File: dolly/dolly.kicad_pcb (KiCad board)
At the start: 2 copper layers, 71.1 x 62.2 mm, 67 parts, among them J1 USB_OTG, J10 X_End, J11 Y_End, J12 Z_End, J13 GS2, J14 GS2, J15 GS2, J16 GS2, J17 GS2, J18 GS2, J19 GS2, J2 Barrel_Jack, J20 GS2, J21 GS2, J22 X_Stepper, J23 Y_Stepper, J24 Z_Stepper, J3 UART, J4 RX, J5 TX, J6 24V_Out, J7 Probe, J8 Spindle, J9 ICSP, SW1 SW_SPST, U1 ATMEGA328PB-AU, U2 CH340G, U3 L7805, U4 AP1117-15, U5 ITEAD_HC-05, Y1 12M, Y2 16M

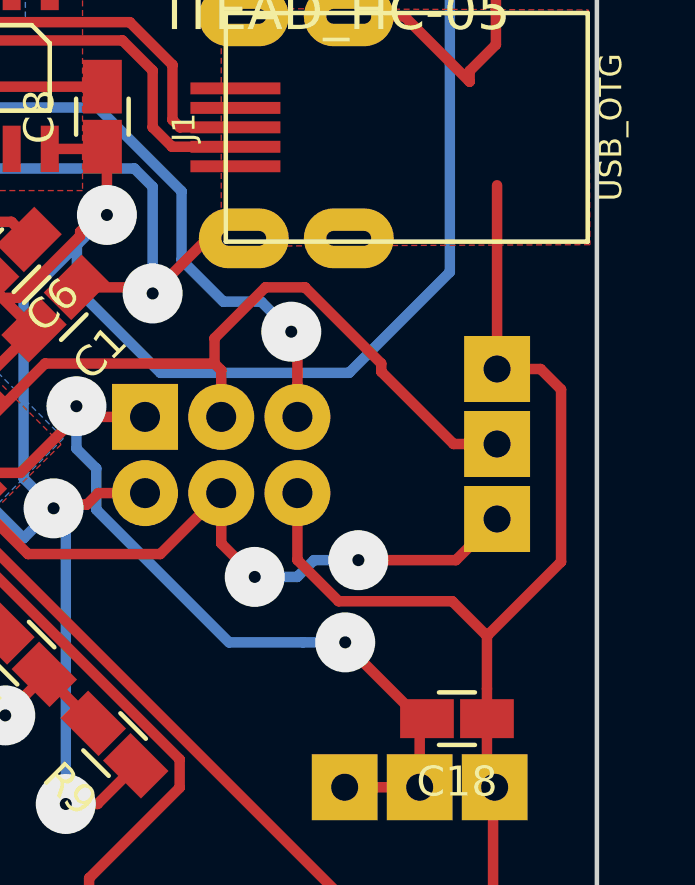
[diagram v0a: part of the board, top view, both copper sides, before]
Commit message: Adding optional 0.1uF capacitors between spindle direction/pwm pins and gnd.
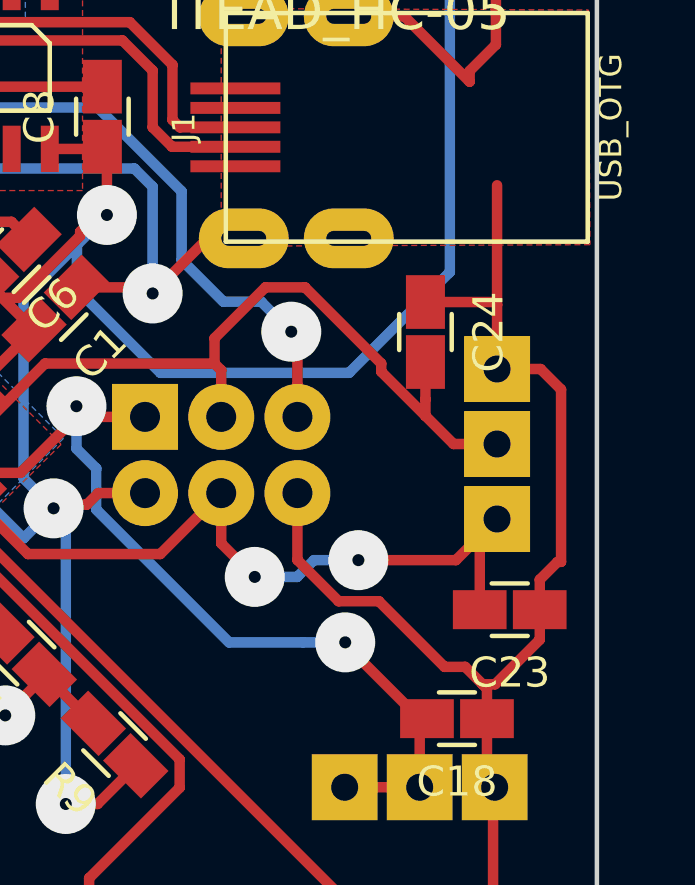
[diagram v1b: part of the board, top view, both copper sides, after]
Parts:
- added C23: 0.1u, coddingtonbear:0805_Milling, F.Cu at (202.2, 117.5)
- added C24: 0.1u, coddingtonbear:0805_Milling, F.Cu at (199.4, 108.2)
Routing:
- net GND: track 453.2 -> 456.6 mm
- net MOSI: track 22.4 -> 25.7 mm
- net SCK: track 23.7 -> 25.4 mm
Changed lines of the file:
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@@
     (thickness 1.6)
     (drawings 6)
-    (tracks 793)
+    (tracks 808)
     (zones 0)
-    (modules 67)
+    (modules 69)
     (nets 108)
   )
@@
     (add_net ~ENABLE_STEPPER)
   )
+  (module coddingtonbear:0805_Milling (layer F.Cu)
+    (at 199.39 108.22 270)
+    (descr "Resistor SMD 0805, reflow soldering, Vishay (see dcrcw.pdf)")
+    (tags "resistor 0805")
+    (attr smd)
+    (fp_text reference C24 (at 0 -2.1 270) (layer F.SilkS)
+      (effects (font (size 1 1) (thickness 0.15)))
+    )
+    (fp_text value 0.1u (at 0 2.1 270) (layer F.Fab)
+      (effects (font (size 1 1) (thickness 0.15)))
+    )
+    (fp_line (start 0.6 0.875) (end -0.6 0.875) (layer F.SilkS) (width 0.15))
+    (fp_line (start -0.6 -0.875) (end 0.6 -0.875) (layer F.SilkS) (width 0.15))
+    (pad 1 smd rect (at -1 0 270) (size 1.79 1.3) (layers F.Cu F.Paste F.Mask)
+      (net 5 GND))
+    (pad 2 smd rect (at 1 0 270) (size 1.79 1.3) (layers F.Cu F.Paste F.Mask)
+      (net 17 SCK))
+    (model Resistors_SMD.3dshapes/R_0805.wrl
+      (at (xyz 0 0 0))
+      (scale (xyz 1 1 1))
+      (rotate (xyz 0 0 0))
+    )
+  )
+  (module coddingtonbear:0805_Milling (layer F.Cu)
+    (at 202.2 117.475 180)
+    (descr "Resistor SMD 0805, reflow soldering, Vishay (see dcrcw.pdf)")
+    (tags "resistor 0805")
+    (attr smd)
+    (fp_text reference C23 (at 0 -2.1 180) (layer F.SilkS)
+      (effects (font (size 1 1) (thickness 0.15)))
+    )
+    (fp_text value 0.1u (at 0 2.1 180) (layer F.Fab)
+      (effects (font (size 1 1) (thickness 0.15)))
+    )
+    (fp_line (start -0.6 -0.875) (end 0.6 -0.875) (layer F.SilkS) (width 0.15))
+    (fp_line (start 0.6 0.875) (end -0.6 0.875) (layer F.SilkS) (width 0.15))
+    (pad 2 smd rect (at 1 0 180) (size 1.79 1.3) (layers F.Cu F.Paste F.Mask)
+      (net 15 MOSI))
+    (pad 1 smd rect (at -1 0 180) (size 1.79 1.3) (layers F.Cu F.Paste F.Mask)
+      (net 5 GND))
+    (model Resistors_SMD.3dshapes/R_0805.wrl
+      (at (xyz 0 0 0))
+      (scale (xyz 1 1 1))
+      (rotate (xyz 0 0 0))
+    )
+  )
   (module celeritous/KiCad.pretty:CAPACITOR_TANTALUM_C (layer F.Cu)
     (at 164.465 76.835 180)
@@
   (segment (start 190.0428 113.5888) (end 188.487166 113.5888) (width 0.35) (layer F.Cu) (net 4))
   (segment (start 188.487166 113.5888) (end 188.106166 113.9698) (width 0.35) (layer F.Cu) (net 4))
+  (segment (start 203.2 117.475) (end 203.2 116.475) (width 0.35) (layer F.Cu) (net 5))
+  (segment (start 203.2 116.475) (end 203.794234 115.880766) (width 0.35) (layer F.Cu) (net 5))
+  (segment (start 203.794234 115.880766) (end 203.9112 115.880766) (width 0.35) (layer F.Cu) (net 5))
+  (segment (start 200.7136 119.38) (end 201.295 119.9614) (width 0.35) (layer F.Cu) (net 5))
+  (segment (start 201.295 119.9614) (end 201.4408 120.1072) (width 0.35) (layer F.Cu) (net 5))
+  (segment (start 203.2 117.475) (end 203.2 118.475) (width 0.35) (layer F.Cu) (net 5))
+  (segment (start 201.7136 119.9614) (end 201.295 119.9614) (width 0.35) (layer F.Cu) (net 5))
+  (segment (start 203.2 118.475) (end 201.7136 119.9614) (width 0.35) (layer F.Cu) (net 5))
+  (segment (start 200.025 119.38) (end 200.7136 119.38) (width 0.35) (layer F.Cu) (net 5))
+  (segment (start 197.839001 117.194001) (end 200.025 119.38) (width 0.35) (layer F.Cu) (net 5))
+  (segment (start 196.497199 117.194001) (end 197.839001 117.194001) (width 0.35) (layer F.Cu) (net 5))
+  (segment (start 201.7776 109.4524) (end 201.7776 107.315) (width 0.35) (layer F.Cu) (net 5))
+  (segment (start 201.7776 107.315) (end 201.7776 103.3272) (width 0.35) (layer F.Cu) (net 5))
+  (segment (start 199.39 107.22) (end 201.6826 107.22) (width 0.35) (layer F.Cu) (net 5))
+  (segment (start 201.6826 107.22) (end 201.7776 107.315) (width 0.35) (layer F.Cu) (net 5))
   (segment (start 179.500731 106.517587) (end 180.858013 106.517587) (width 0.35) (layer B.Cu) (net 5))
   (segment (start 180.858013 106.517587) (end 182.9816 104.394) (width 0.35) (layer B.Cu) (net 5))
@@
   (segment (start 190.2968 106.934) (end 190.2968 103.378) (width 0.35) (layer B.Cu) (net 5))
   (segment (start 183.981599 103.394001) (end 182.9816 104.394) (width 0.35) (layer B.Cu) (net 5))
-  (segment (start 201.7776 109.4524) (end 201.7776 103.3272) (width 0.35) (layer F.Cu) (net 5))
-  (segment (start 196.497199 117.194001) (end 200.283635 117.194001) (width 0.35) (layer F.Cu) (net 5))
-  (segment (start 200.283635 117.194001) (end 201.4408 118.351166) (width 0.35) (layer F.Cu) (net 5))
   (segment (start 195.1228 113.5888) (end 195.1228 115.819602) (width 0.35) (layer F.Cu) (net 5))
   (segment (start 195.1228 115.819602) (end 196.497199 117.194001) (width 0.35) (layer F.Cu) (net 5))
   (segment (start 203.9112 110.136) (end 203.9112 115.880766) (width 0.35) (layer F.Cu) (net 5))
-  (segment (start 203.9112 115.880766) (end 201.4408 118.351166) (width 0.35) (layer F.Cu) (net 5))
   (segment (start 201.7776 109.4524) (end 203.2276 109.4524) (width 0.35) (layer F.Cu) (net 5))
   (segment (start 203.2276 109.4524) (end 203.9112 110.136) (width 0.35) (layer F.Cu) (net 5))
-  (segment (start 201.4408 118.351166) (end 201.4408 120.1072) (width 0.35) (layer F.Cu) (net 5))
   (segment (start 201.4408 120.1072) (end 201.4408 121.1072) (width 0.35) (layer F.Cu) (net 5))
   (segment (start 201.644 129.1844) (end 201.644 123.4468) (width 0.35) (layer F.Cu) (net 5))
@@
   (segment (start 199.2484 129.58) (end 199.644 129.1844) (width 0.35) (layer F.Cu) (net 14))
   (segment (start 196.7484 131.572) (end 199.2484 131.572) (width 0.35) (layer F.Cu) (net 14))
+  (segment (start 201.2 117.475) (end 201.2 115.03) (width 0.35) (layer F.Cu) (net 15))
+  (segment (start 201.2 115.03) (end 201.7776 114.4524) (width 0.35) (layer F.Cu) (net 15))
   (segment (start 197.1548 115.824) (end 200.406 115.824) (width 0.35) (layer F.Cu) (net 15))
   (segment (start 200.406 115.824) (end 201.7776 114.4524) (width 0.35) (layer F.Cu) (net 15))
@@
   (segment (start 187.7568 111.0488) (end 190.0428 111.0488) (width 0.35) (layer F.Cu) (net 16))
   (segment (start 184.564405 112.913607) (end 185.891993 112.913607) (width 0.35) (layer F.Cu) (net 16))
+  (segment (start 197.9168 109.5416) (end 199.39 111.0148) (width 0.35) (layer F.Cu) (net 17))
+  (segment (start 199.39 111.0148) (end 200.3276 111.9524) (width 0.35) (layer F.Cu) (net 17))
+  (segment (start 199.39 109.22) (end 199.39 110.465) (width 0.35) (layer F.Cu) (net 17))
+  (segment (start 199.39 110.465) (end 199.39 111.0148) (width 0.35) (layer F.Cu) (net 17))
   (segment (start 195.3768 106.7308) (end 197.9168 109.2708) (width 0.35) (layer F.Cu) (net 17))
   (segment (start 194.056 106.7308) (end 195.3768 106.7308) (width 0.35) (layer F.Cu) (net 17))
@@
   (segment (start 192.360434 109.2708) (end 192.360434 108.426366) (width 0.35) (layer F.Cu) (net 17))
   (segment (start 197.9168 109.2708) (end 197.9168 109.5416) (width 0.35) (layer F.Cu) (net 17))
-  (segment (start 197.9168 109.5416) (end 200.3276 111.9524) (width 0.35) (layer F.Cu) (net 17))
   (segment (start 200.3276 111.9524) (end 201.7776 111.9524) (width 0.35) (layer F.Cu) (net 17))
   (segment (start 184.564405 110.961993) (end 185.017958 110.961993) (width 0.35) (layer F.Cu) (net 17))
